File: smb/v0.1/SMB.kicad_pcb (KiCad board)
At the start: 2 copper layers, 100 x 86 mm, 91 parts, among them IC1 MAX485, IC101 ATMEGA1284-A, J101 RJ45, J102 RTS_RESET, J103 ICSP, J104 SERIAL_REV, J202 USD_CONN, J401 HR911105_RJ45, P1 CONN_2, P101 I2C_CONN, P102 CONN_3X2, P103 CONN_3X2, P104 CONN_3X2, P105 CONN_5, P106 CONN_3X2, P107 CONN_3, P108 CONN_5, P301 CONN_2, SW101 SKQGAKE010, U201 ENC28J60, U202 LM1117IMP-3.3, U301 74HC08, U302 MP2562DS, U303 74HC08, X101 20MHz, X201 25MHz

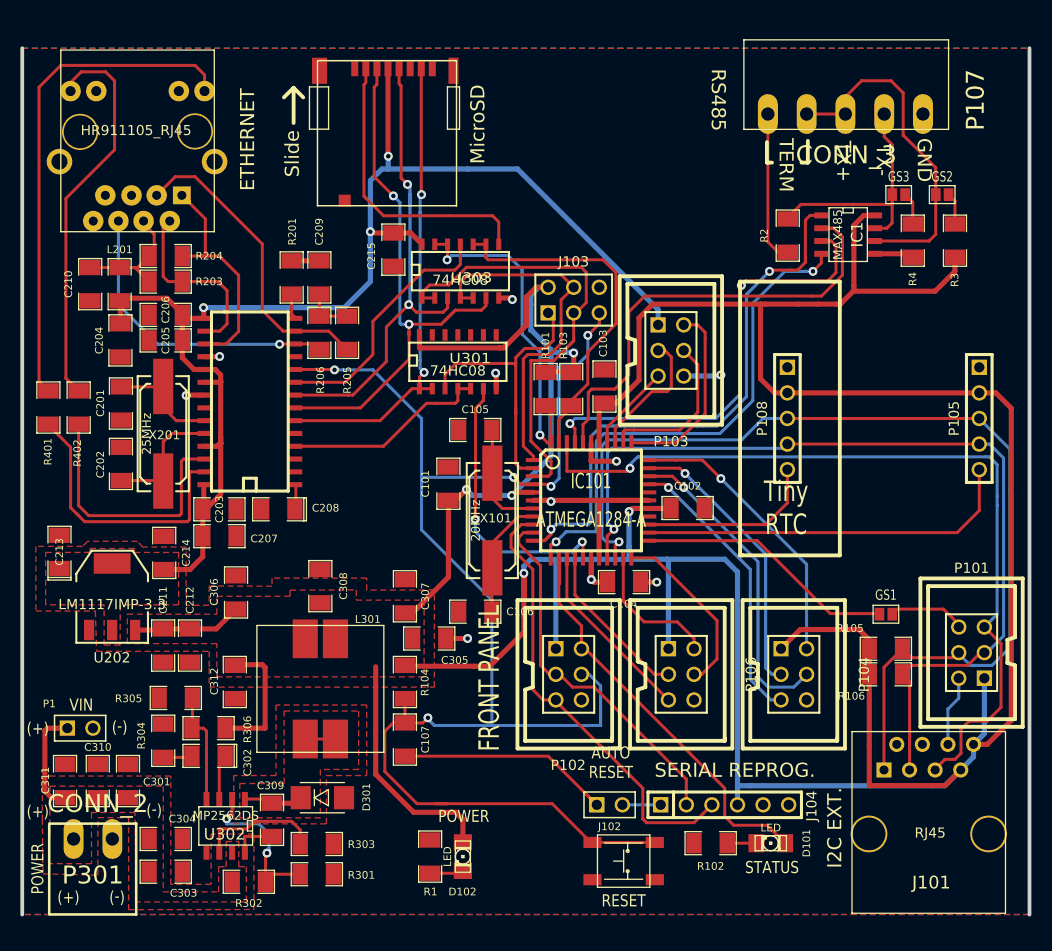
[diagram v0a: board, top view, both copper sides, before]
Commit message: ajout gateway onewire DS2482-100 + connecteur 3 points deplacement connecteurs pour amelioration branchement remplacement connecteur 5 points rs485 par 3 points + un strap pour resistance de terminaison
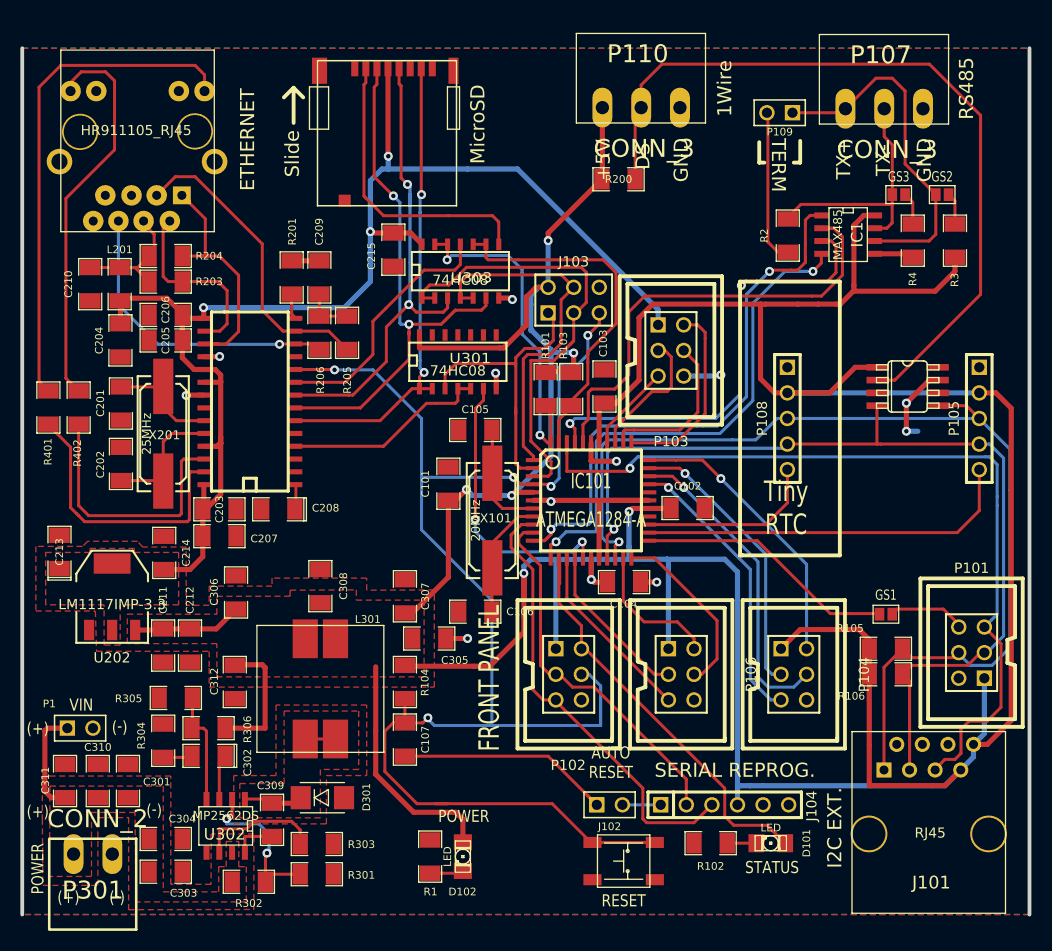
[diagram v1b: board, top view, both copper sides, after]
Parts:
- added IC2: DS2482-100S, 1wire-SO08, F.Cu at (120.9, 60.6)
- added P109: CONN_3, PIN_ARRAY_2X1, F.Cu at (108.2, 33.4)
- added P110: CONN_3, MOL_CONN_3_MINI, F.Cu at (98.3, 32.9)
- added R200: 4.7k, SM1206, F.Cu at (92.2, 40.0)
- P107: footprint MOL_CONN_5_MINI -> MOL_CONN_3_MINI
- moved P301 1.50 mm to (40.0, 107.0)
- moved P107 0.53 mm to (122.4, 33.0)
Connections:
- R2 pad 2: N-0000021 -> N-0000030
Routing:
- net N-0000029: track 0.00 -> 77.9 mm
- net +5V: track 418.1 -> 448.1 mm, vias 6 -> 7
- net N-0000030: track 0.00 -> 15.1 mm
- net N-0000021: track 15.1 -> 0.00 mm
- net SDA: track 101.2 -> 105.8 mm
- net SCL: track 90.9 -> 94.7 mm
- net GND: track 55.3 -> 56.4 mm, vias 9 -> 11
- net TX+: track 34.1 -> 34.9 mm
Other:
- board text added: "+5V"
- board text added: "1Wire"
- board text added: "DS"

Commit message: ajout trou de fixation reprise connecteur 2x10 pour extension deplacement slot I2C ...
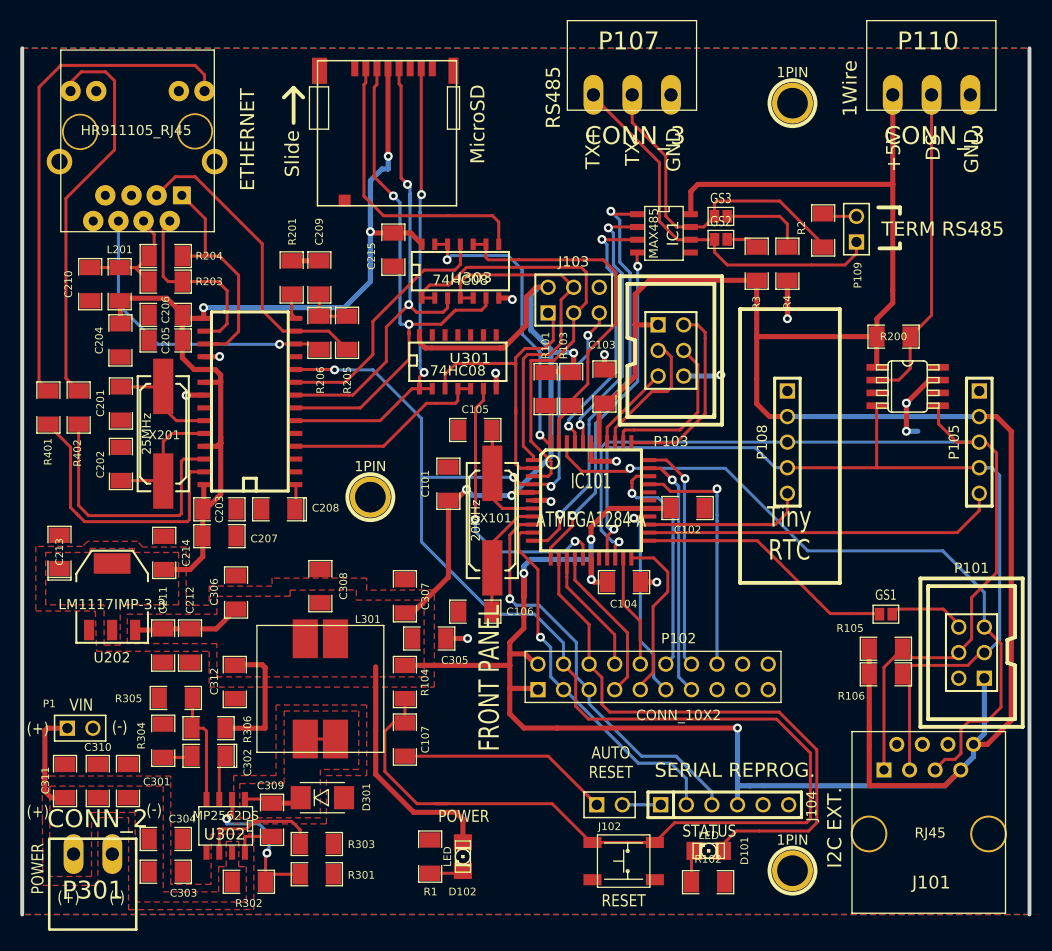
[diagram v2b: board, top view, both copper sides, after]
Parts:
- removed P104, P106: CONN_3X2, HE10-6
- added 1PIN: P***, 1pin, F.Cu at (109.5, 108.6)
- added 1PIN: P***, 1pin, F.Cu at (67.6, 71.6)
- added 1PIN: P***, 1pin, F.Cu at (109.5, 32.4)
- P102: value CONN_3X2 -> CONN_10X2; footprint HE10-6 -> pin_array_10x2
- moved R200 31.5 mm to (119.5, 55.6)
- moved P110 28.9 mm to (127.1, 31.6)
- moved P107 25.1 mm to (97.4, 31.6)
- moved GS2 22.4 mm to (102.4, 46.0)
- moved R3 19.8 mm to (105.9, 48.4)
- moved IC1 18.3 mm to (96.7, 45.4)
- moved GS3 17.8 mm to (102.4, 43.7)
- moved P109 13.8 mm to (115.8, 45.0), turned to 90 degrees
- moved R4 12.7 mm to (109.0, 48.4)
- moved P102 10.9 mm to (98.2, 89.4), turned to 0 degrees
- moved D101 6.21 mm to (101.2, 106.7)
- moved R102 3.88 mm to (101.1, 109.8), turned to 0 degrees
- moved R2 3.56 mm to (112.5, 45.1), turned to 90 degrees
- moved P105 2.35 mm to (128.0, 66.1)
- moved P108 2.35 mm to (109.0, 66.1)
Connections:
- IC101 pad 26: N-0000027 -> PC7
- P102 pad 2: LED_STATUS -> +5V
- P102 pad 6: GND -> LED_STATUS
- P103 pad 1: 3.3V -> +5V
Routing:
- net N-000004: track 77.9 -> 31.9 mm
- net 3.3V: track 131.6 -> 97.5 mm
- net /RESET: track 148.0 -> 173.6 mm, vias 5 -> 4
- net GND: track 56.4 -> 36.1 mm, vias 11 -> 13
- net PC7: track 0.00 -> 19.9 mm, vias 0 -> 1
- net PB0: track 46.4 -> 26.8 mm, vias 0 -> 2
- net PB1: track 45.3 -> 26.5 mm
- net TX1: track 51.6 -> 33.9 mm
- net LED_STATUS: track 42.4 -> 58.1 mm
- net RX1: track 57.3 -> 41.8 mm
- net +5V: track 448.1 -> 433.0 mm
- net N-000005: track 15.1 -> 3.41 mm
- net /INT_I2C: track 82.4 -> 71.1 mm
- net TX-: track 24.6 -> 33.6 mm
- net PA6: track 31.6 -> 23.3 mm
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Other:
- board text added: "TERM RS485"
- board text removed: "TERM"

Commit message: generation gerber controle et optimisation routage ajout empreinte TO92 pour ds18b20 ajout i2c sur connecteur d'extension
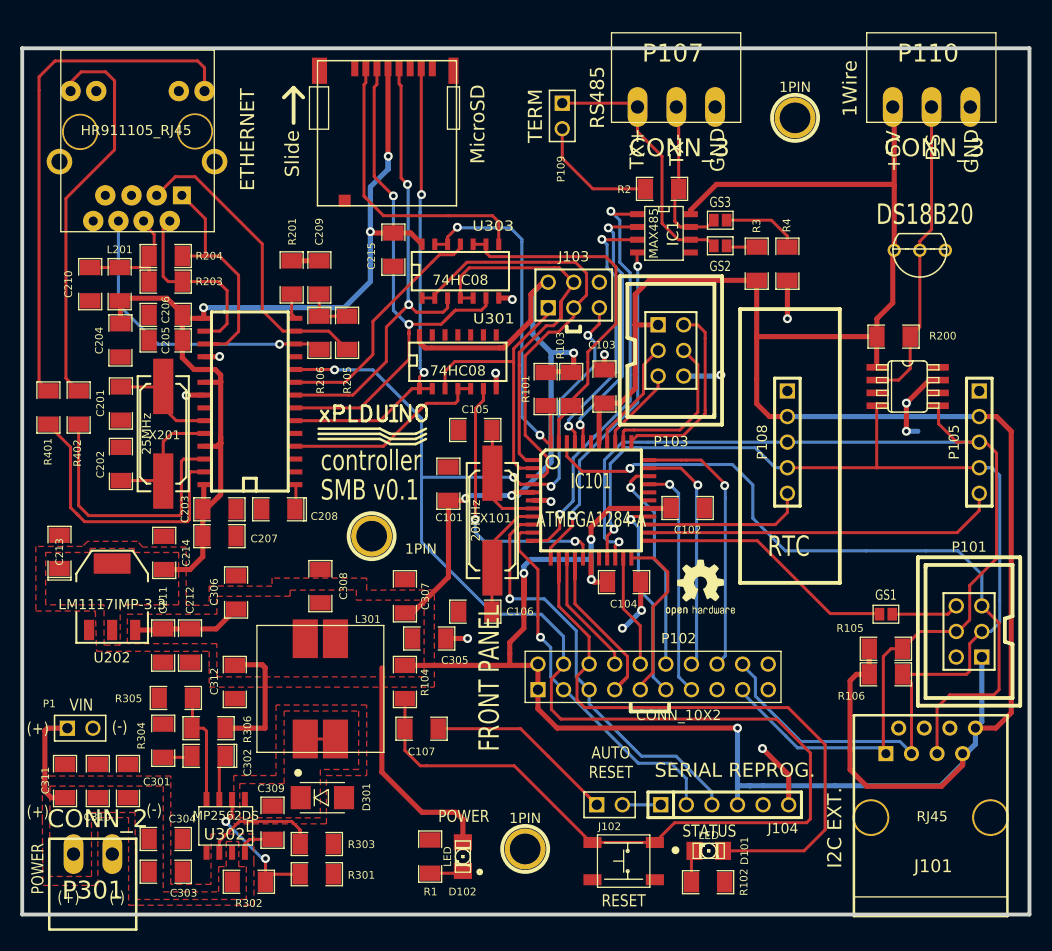
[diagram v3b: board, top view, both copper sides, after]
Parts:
- removed the 1PIN at (109.5, 108.6)
- removed the 1PIN at (67.6, 71.6)
- removed the 1PIN at (109.5, 32.4)
- added 1PIN: P***, 1pin, F.Cu at (67.7, 75.4)
- added 1PIN: P***, 1pin, F.Cu at (109.7, 33.9)
- added 1PIN: P***, 1pin, F.Cu at (82.9, 106.5)
- added G***: LOGO, OSHWLOGO0.3IN, F.Cu at (96.5, 76.8)
- added P2: CONN_3, 1wire-TO92-, F.Cu at (122.1, 47.1)
- added logo_xplduino: VAL**, logo_xplduino, F.Cu at (67.8, 65.0)
- moved P109 31.3 mm to (86.6, 33.7), turned to 270 degrees
- moved R2 16.5 mm to (96.5, 41.0), turned to 180 degrees
- moved P107 4.54 mm to (101.8, 32.8)
- moved P101 2.12 mm to (127.0, 84.9)
- moved C107 1.97 mm to (72.6, 94.6), turned to 180 degrees
- moved J101 1.63 mm to (123.2, 103.4)
- moved P110 1.21 mm to (127.1, 32.8)
- moved GS2 0.64 mm to (102.3, 46.6)
- moved J103 0.50 mm to (87.8, 51.5)
- moved GS3 0.39 mm to (102.3, 44.1)
- moved C309 0.29 mm to (57.8, 103.9)
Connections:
- P102 pad 13: PA5 -> PA7
- P102 pad 14: PA4 -> PA5
- P102 pad 16: PA7 -> PA4
- P102 pad 17: N-0000048 -> SDA
- P102 pad 18: N-0000049 (its old number) -> SCL
- P103 pad 3: PA1 -> PA0
- P103 pad 5: PA0 -> PA1
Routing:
- net SCL: track 97.0 -> 116.2 mm
- net TX-: track 33.6 -> 16.0 mm
- net SDA: track 99.6 -> 112.8 mm
- net TX+: track 39.0 -> 26.4 mm
- net N-000003: track 3.41 -> 12.4 mm
- net LED_STATUS: track 58.1 -> 67.0 mm
- net PD6: track 15.8 -> 23.5 mm
- net GND: track 36.1 -> 42.3 mm, vias 13 -> 14
- net PA1: track 13.5 -> 8.39 mm
- net pre_5V: track 8.95 -> 4.37 mm
- net SPI_CLK: track 48.0 -> 43.8 mm
- net PA4: track 23.0 -> 26.8 mm
- net +5V: track 433.0 -> 429.7 mm
- net /RESET: track 173.6 -> 170.4 mm
- net SPI_MOSI: track 36.2 -> 38.9 mm
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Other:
- board text added: "DS18B20"
- board text added: "RTC"
- board text added: "SMB v0.1"
- board text added: "TERM"
- board text added: "controller"
- board text removed: "TERM RS485"
- board text removed: "Tiny RTC"

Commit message: suppression pin DS du slot RTC (inutile depuis l'installation d'un DS2408) ajout led 'fault'
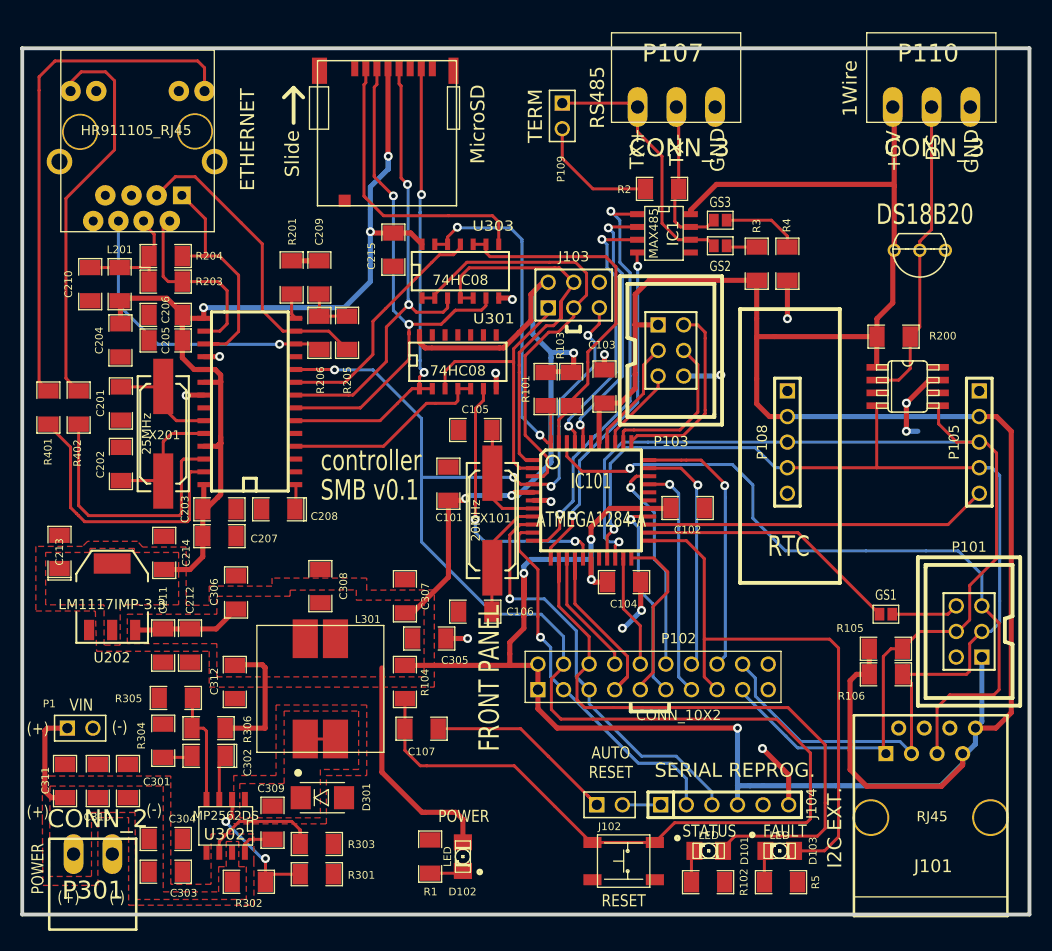
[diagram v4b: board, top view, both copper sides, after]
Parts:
- removed 1PIN (x3): P***, 1pin
- removed G***: LOGO, OSHWLOGO0.3IN
- removed logo_xplduino: VAL**, logo_xplduino
- added D103: LED, LED-1206, F.Cu at (108.2, 106.7)
- added R5: 3.3kR, SM1206, F.Cu at (108.3, 109.8)
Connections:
- GS1 pad 2: N-0000035 -> N-0000038
- IC101 pad 23: N-0000035 -> LED_FAULT
- IC101 pad 24: PC5 -> N-0000038
- IC101 pad 25: DS -> PC6
- P102 pad 15: N-0000049 -> LED_FAULT
- P105 pad 5: PC5 -> PC6
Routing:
- net LED_FAULT: track 0.00 -> 57.2 mm
- net PC5: track 35.4 -> 0.00 mm
- net PC6: track 0.00 -> 34.1 mm
- net N-0000038: track 0.00 -> 26.3 mm
- net N-0000035: track 26.0 -> 0.00 mm
- net DS: track 16.3 -> 0.00 mm
- net N-0000029: track 0.00 -> 3.15 mm
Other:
- board text added: "FAULT"

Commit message: mis au pas 2.54 ecartement slot i2c inversion connecteur FTDI/leds
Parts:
- added G***: LOGO, OSHWLOGO0.3IN, F.Cu at (71.6, 101.9)
- added logo_xplduino: VAL**, logo_xplduino, F.Cu at (68.1, 64.8)
- moved R1 25.2 mm to (97.0, 98.3), turned to 0 degrees
- moved D102 20.9 mm to (97.0, 102.4), turned to 180 degrees
- moved R102 14.4 mm to (109.7, 98.3)
- moved R5 12.5 mm to (103.4, 98.3)
- moved D101 9.60 mm to (109.7, 102.4)
- moved D103 6.48 mm to (103.4, 102.4)
- moved J104 5.97 mm to (102.8, 108.1)
- moved SW101 3.06 mm to (89.7, 108.0)
- moved J102 1.73 mm to (89.7, 102.6)
- moved P105 0.95 mm to (127.1, 66.1)
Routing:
- net /RESET: track 170.4 -> 131.2 mm, vias 4 -> 5
- net LED_STATUS: track 67.1 -> 49.2 mm
- net +5V: track 429.7 -> 420.3 mm
- net TX0: track 37.2 -> 44.9 mm, vias 1 -> 0
- net GND: track 42.3 -> 35.2 mm, vias 14 -> 13
- net LED_FAULT: track 57.2 -> 62.2 mm
- net N-000004: track 3.81 -> 8.57 mm
- net PD6: track 23.5 -> 19.9 mm
- net RX0: track 43.7 -> 45.3 mm
- net N-0000010: track 20.2 -> 18.7 mm
- net SCL: track 116.2 -> 117.2 mm
- net N-0000029: track 3.15 -> 4.16 mm
- net SDA: track 112.8 -> 111.9 mm
- net N-0000052: track 3.35 -> 4.16 mm
- net N-0000051: track 3.65 -> 4.16 mm
